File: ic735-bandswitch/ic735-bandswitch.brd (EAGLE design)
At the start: 94 x 71 mm, 26 parts, among them IC2 ARDUINO_PRO_MICRO

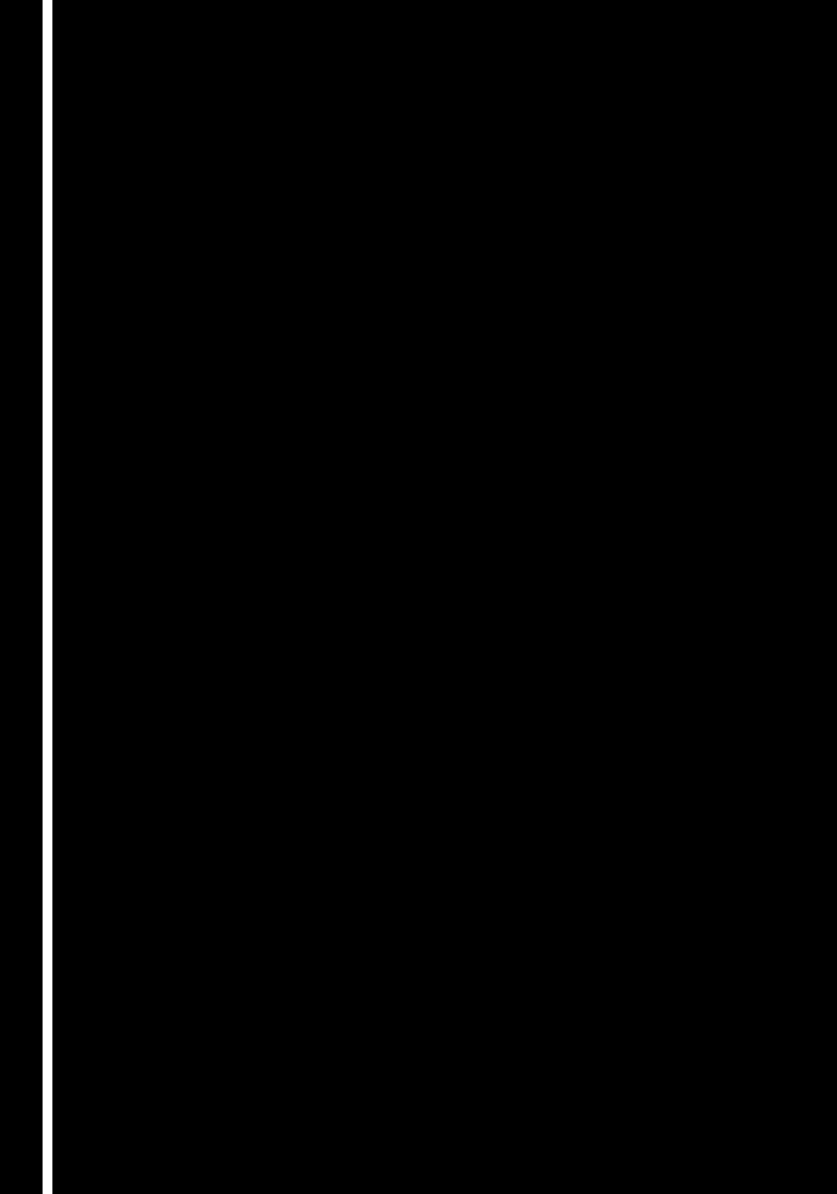
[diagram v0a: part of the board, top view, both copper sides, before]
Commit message: Add rotary switch and pdf
Add rotary switch for better understanding.
Add PDF files.
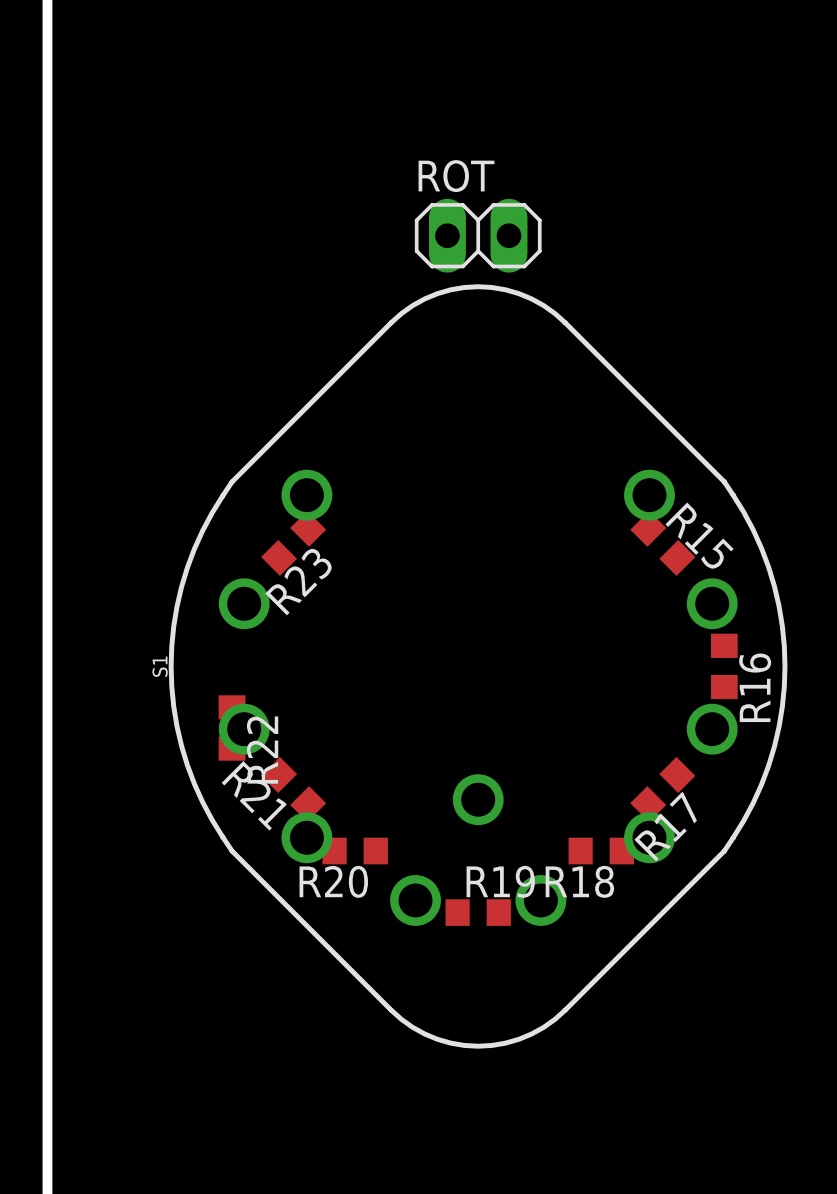
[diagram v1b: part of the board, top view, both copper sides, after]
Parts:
- added R15, R16, R17, R18, R19, R20, R21, R22, R23: (no value), rcl:R0603
- added ROT: (no value), pinhead:1X02
- added S1: ROTARY 1X10, SparkFun-Switches:ROTARY_SWITCH_1X10
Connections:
- net +8V renamed +8V_REF
- new net N$32: R15.1, S1.1
- new net N$33: R15.2, R16.1, S1.2
- new net N$34: R23.1, ROT.1, S1.10
- new net N$35: R16.2, R17.1, S1.3
- new net N$36: R19.1, R20.1, S1.6
- new net N$37: R17.2, R18.1, S1.4
- new net N$38: R18.2, R19.2, S1.5
- new net N$39: ROT.2, S1.COMMON
- new net N$40: R20.2, R21.1, S1.7
- new net N$41: R21.2, R22.2, S1.8
- new net N$42: R22.1, R23.2, S1.9
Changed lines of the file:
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@@
 <element name="C4" library="rcl" package="C025-024X044" value="" x="0" y="-59.69" rot="R270"/>
 <element name="C1" library="rcl" package="E2,5-6E" value="" x="-10.16" y="-59.69" rot="R270"/>
+<element name="S1" library="SparkFun-Switches" package="ROTARY_SWITCH_1X10" value="ROTARY 1X10" x="27.94" y="-43.18">
+<attribute name="PROD_ID" value="SWCH-12120" x="27.94" y="-43.18" size="1.778" layer="27" display="off"/>
+<attribute name="SF_SKU" value="COM-13253" x="27.94" y="-43.18" size="1.778" layer="27" display="off"/>
+</element>
+<element name="R15" library="rcl" package="R0603" value="" x="35.56" y="-38.1" rot="R315"/>
+<element name="R16" library="rcl" package="R0603" value="" x="38.1" y="-43.18" rot="R270"/>
+<element name="R17" library="rcl" package="R0603" value="" x="35.56" y="-48.26" rot="R225"/>
+<element name="R18" library="rcl" package="R0603" value="" x="33.02" y="-50.8" rot="R180"/>
+<element name="R19" library="rcl" package="R0603" value="" x="27.94" y="-53.34"/>
+<element name="R20" library="rcl" package="R0603" value="" x="22.86" y="-50.8" rot="R180"/>
+<element name="R21" library="rcl" package="R0603" value="" x="20.32" y="-48.26" rot="R135"/>
+<element name="R22" library="rcl" package="R0603" value="" x="17.78" y="-45.72" rot="R270"/>
+<element name="R23" library="rcl" package="R0603" value="" x="20.32" y="-38.1" rot="R225"/>
+<element name="ROT" library="pinhead" package="1X02" value="" x="27.94" y="-25.4"/>
 </elements>
 <signals>
@@
 <wire x1="0" y1="-58.42" x2="0" y2="-53.34" width="0.6096" layer="16"/>
 </signal>
-<signal name="+8V">
+<signal name="+8V_REF">
 <contactref element="ACC2" pad="1"/>
 <contactref element="R11" pad="2"/>
@@
 <wire x1="-10.16" y1="0" x2="-12.7" y2="0" width="0" layer="19" extent="1-1"/>
 </signal>
+<signal name="N$32">
+<contactref element="R15" pad="1"/>
+<contactref element="S1" pad="1"/>
+<wire x1="35.01106875" y1="-36.10893125" x2="34.95895625" y2="-37.49895625" width="0" layer="19" extent="1-1"/>
+</signal>
+<signal name="N$33">
+<contactref element="R15" pad="2"/>
+<contactref element="S1" pad="2"/>
+<contactref element="R16" pad="1"/>
+<wire x1="36.161040625" y1="-38.701040625" x2="38.1" y2="-42.33" width="0" layer="19" extent="1-1"/>
+<wire x1="37.599259375" y1="-40.591809375" x2="36.161040625" y2="-38.701040625" width="0" layer="19" extent="1-1"/>
+</signal>
+<signal name="N$35">
+<contactref element="R17" pad="1"/>
+<contactref element="S1" pad="3"/>
+<contactref element="R16" pad="2"/>
+<wire x1="38.1" y1="-44.03" x2="36.161040625" y2="-47.65895625" width="0" layer="19" extent="1-1"/>
+<wire x1="37.599259375" y1="-45.768190625" x2="38.1" y2="-44.03" width="0" layer="19" extent="1-1"/>
+</signal>
+<signal name="N$37">
+<contactref element="S1" pad="4"/>
+<contactref element="R17" pad="2"/>
+<contactref element="R18" pad="1"/>
+<wire x1="34.95895625" y1="-48.861040625" x2="33.87" y2="-50.8" width="0" layer="19" extent="1-1"/>
+<wire x1="35.01106875" y1="-50.25106875" x2="34.95895625" y2="-48.861040625" width="0" layer="19" extent="1-1"/>
+</signal>
+<signal name="N$38">
+<contactref element="S1" pad="5"/>
+<contactref element="R18" pad="2"/>
+<contactref element="R19" pad="2"/>
+<wire x1="32.17" y1="-50.8" x2="28.79" y2="-53.34" width="0" layer="19" extent="1-1"/>
+<wire x1="30.528190625" y1="-52.839259375" x2="32.17" y2="-50.8" width="0" layer="19" extent="1-1"/>
+</signal>
+<signal name="N$36">
+<contactref element="S1" pad="6"/>
+<contactref element="R19" pad="1"/>
+<contactref element="R20" pad="1"/>
+<wire x1="27.09" y1="-53.34" x2="23.71" y2="-50.8" width="0" layer="19" extent="1-1"/>
+<wire x1="25.351809375" y1="-52.839259375" x2="27.09" y2="-53.34" width="0" layer="19" extent="1-1"/>
+</signal>
+<signal name="N$40">
+<contactref element="S1" pad="7"/>
+<contactref element="R20" pad="2"/>
+<contactref element="R21" pad="1"/>
+<wire x1="22.01" y1="-50.8" x2="20.921040625" y2="-48.861040625" width="0" layer="19" extent="1-1"/>
+<wire x1="20.86893125" y1="-50.25106875" x2="22.01" y2="-50.8" width="0" layer="19" extent="1-1"/>
+</signal>
+<signal name="N$41">
+<contactref element="S1" pad="8"/>
+<contactref element="R21" pad="2"/>
+<contactref element="R22" pad="2"/>
+<wire x1="19.71895625" y1="-47.65895625" x2="17.78" y2="-46.57" width="0" layer="19" extent="1-1"/>
+<wire x1="18.280740625" y1="-45.768190625" x2="19.71895625" y2="-47.65895625" width="0" layer="19" extent="1-1"/>
+</signal>
+<signal name="N$42">
+<contactref element="S1" pad="9"/>
+<contactref element="R22" pad="1"/>
+<contactref element="R23" pad="2"/>
+<wire x1="17.78" y1="-44.87" x2="19.71895625" y2="-38.701040625" width="0" layer="19" extent="1-1"/>
+<wire x1="18.280740625" y1="-40.591809375" x2="17.78" y2="-44.87" width="0" layer="19" extent="1-1"/>
+</signal>
+<signal name="N$34">
+<contactref element="S1" pad="10"/>
+<contactref element="R23" pad="1"/>
+<contactref element="ROT" pad="1"/>
+<wire x1="20.921040625" y1="-37.49895625" x2="26.67" y2="-25.4" width="0" layer="19" extent="1-1"/>
+<wire x1="20.86893125" y1="-36.10893125" x2="20.921040625" y2="-37.49895625" width="0" layer="19" extent="1-1"/>
+</signal>
+<signal name="N$39">
+<contactref element="S1" pad="COMMON"/>
+<contactref element="ROT" pad="2"/>
+<wire x1="27.94" y1="-48.68" x2="29.21" y2="-25.4" width="0" layer="19" extent="1-1"/>
+</signal>
 </signals>
